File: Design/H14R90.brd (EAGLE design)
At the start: 34.6 x 30 mm, 39 parts, among them P2 HEXABIT_17.32_NO_P6, Q1 MMBT3904LT1, Q2 MMBT3904LT1, Q3 MMBT3904LT1, Q4 MMBT3904LT1, U1 STM32G0B1CEU6N, U2 LM2775-Q1, X1 XTALL_CSTCE8M00G52

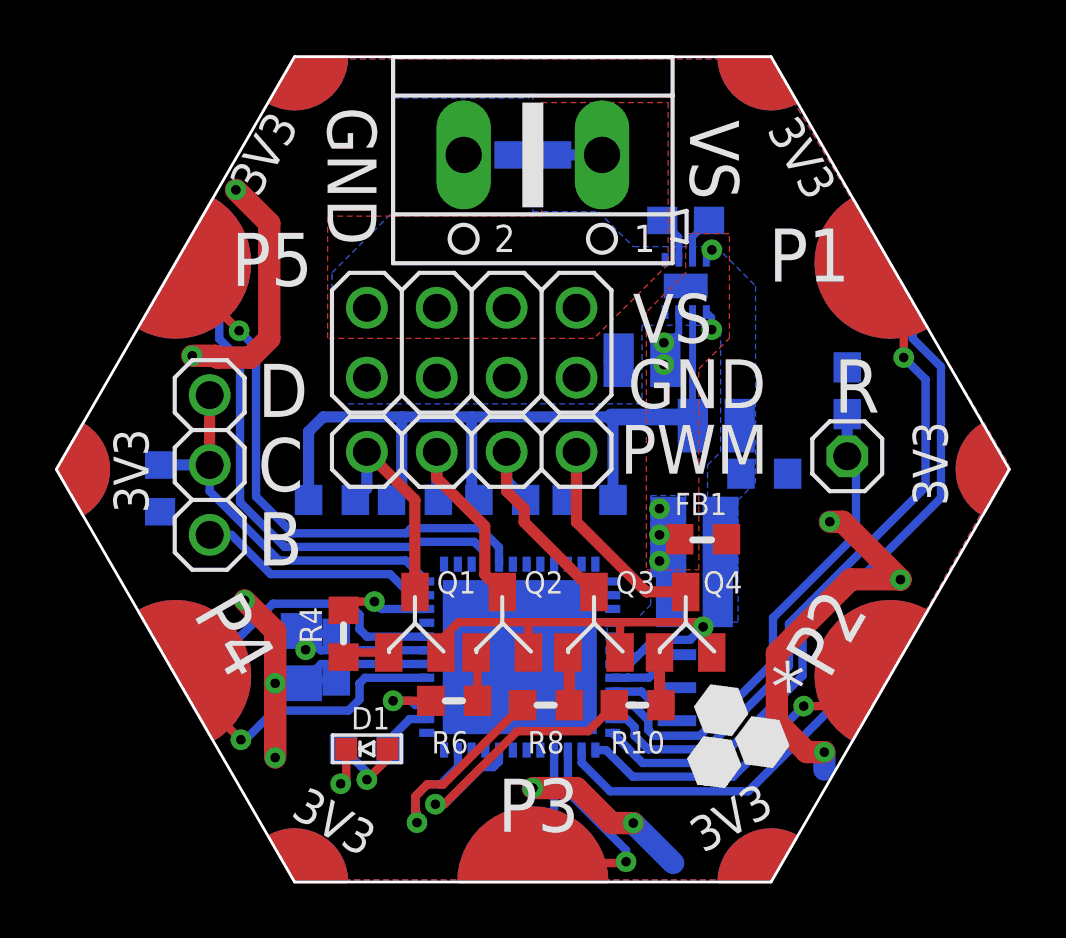
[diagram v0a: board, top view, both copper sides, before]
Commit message: -Fix the outputs pin headers spacing
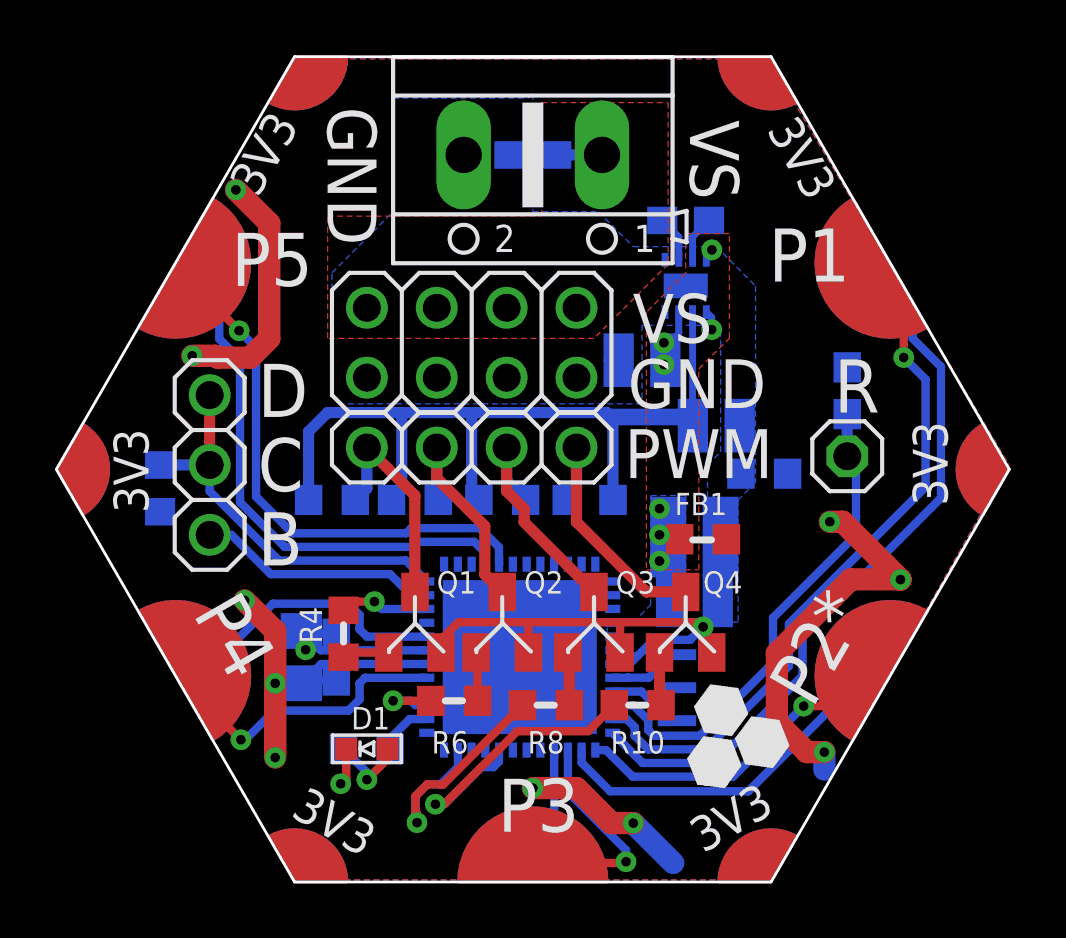
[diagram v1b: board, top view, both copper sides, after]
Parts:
- moved JP1 0.16 mm to (-2.22, 15.9)
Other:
- board text added: "7.2V Max"
- board text added: "P2*"
- board text removed: "*P2"
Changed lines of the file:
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@@
 <text x="8.5725" y="21.9075" size="1.9304" layer="21" rot="SR0">P1</text>
 <text x="11.1125" y="21.74875" size="1.9304" layer="26" rot="SMR0">P1</text>
-<text x="10.16" y="6.35" size="1.9304" layer="21" rot="R60">*P2</text>
-<text x="14.44625" y="9.36625" size="1.9304" layer="26" rot="MR0">*P2</text>
+<text x="10.16" y="6.35" size="1.9304" layer="21" rot="R60">P2*</text>
+<text x="14.12875" y="9.36625" size="1.9304" layer="26" rot="SMR0">P2*</text>
 <text x="-11.1125" y="23.65375" size="1.9304" layer="26" rot="MR180">P5</text>
 <text x="-10.95375" y="21.74875" size="1.9304" layer="21" rot="SR0">P5</text>
 <text x="-12.3825" y="9.8425" size="1.9304" layer="21" rot="SR300">P4</text>
-<text x="-13.6525" y="11.27125" size="1.9304" layer="26" rot="MR180">P4</text>
+<text x="-11.58875" y="9.2075" size="1.9304" layer="26" rot="MR0">P4</text>
 <text x="-1.5875" y="3.81" size="1.9304" layer="26" rot="MR180">P3</text>
 <text x="-1.27" y="1.905" size="1.9304" layer="21">P3</text>
-<text x="-2.2225" y="23.1775" size="1.9304" layer="22" font="vector" rot="MR180" align="center">H14R90</text>
+<text x="-9.8425" y="15.71625" size="1.9304" layer="22" font="vector" rot="MR90" align="center">H14R90</text>
 <text x="-10.00125" y="11.58875" size="1.9304" layer="25">B</text>
 <text x="10.95375" y="17.145" size="1.9304" layer="21">R</text>
@@
 <text x="3.6327875" y="19.685" size="1.778" layer="21">VS</text>
 <text x="3.451703125" y="17.30375" size="1.778" layer="21">GND</text>
-<text x="3.175" y="14.9225" size="1.778" layer="21">PWM</text>
+<text x="3.33375" y="14.76375" size="1.778" layer="21">PWM</text>
 <text x="-7.46125" y="28.2575" size="1.778" layer="21" rot="SR270">GND</text>
 <text x="5.715" y="27.78125" size="1.778" layer="21" rot="SR270">VS</text>
+<text x="-1.11125" y="23.33625" size="1.4224" layer="22" font="vector" rot="MR0" align="center">7.2V Max</text>
+<text x="3.4925" y="28.73375" size="1.27" layer="22" rot="SMR0">VS</text>
+<text x="-1.11125" y="28.73375" size="1.27" layer="22" rot="SMR0">GND</text>
 </plain>
 <attributes>
@@
 <attribute name="MFN" value="" x="-6.0325" y="4.92125" size="1.778" layer="28" rot="MR0" display="off"/>
 <attribute name="MPN" value="" x="-6.0325" y="4.92125" size="1.778" layer="28" rot="MR0" display="off"/>
-<attribute name="NAME" x="-5.3975" y="5.715" size="0.8128" layer="26" rot="MR0"/>
+<attribute name="NAME" x="-5.3975" y="5.55625" size="0.8128" layer="26" rot="MR0"/>
 <attribute name="OCTOPART_URL" value="" x="-6.0325" y="4.92125" size="1.778" layer="28" rot="MR0" display="off"/>
 <attribute name="RESISTANCE" value="" x="-6.0325" y="4.92125" size="1.778" layer="28" rot="MR0" display="off"/>
@@
 <attribute name="MFN" value="" x="-7.14375" y="8.255" size="1.778" layer="28" rot="MR270" display="off"/>
 <attribute name="MPN" value="" x="-7.14375" y="8.255" size="1.778" layer="28" rot="MR270" display="off"/>
-<attribute name="NAME" x="-6.429375" y="7.540625" size="0.8128" layer="26" rot="MR90"/>
+<attribute name="NAME" x="-6.270625" y="7.699375" size="0.8128" layer="26" rot="MR90"/>
 <attribute name="OCTOPART_URL" value="" x="-7.14375" y="8.255" size="1.778" layer="28" rot="MR270" display="off"/>
 <attribute name="TOLERANCE" value="" x="-7.14375" y="8.255" size="1.778" layer="28" rot="MR270" display="off"/>
@@
 <attribute name="MFN" value="" x="-8.41375" y="8.255" size="1.778" layer="28" rot="MR270" display="off"/>
 <attribute name="MPN" value="" x="-8.41375" y="8.255" size="1.778" layer="28" rot="MR270" display="off"/>
-<attribute name="NAME" x="-10.398125" y="7.77875" size="0.8128" layer="26" rot="MR90"/>
+<attribute name="NAME" x="-8.969375" y="5.23875" size="0.8128" layer="26" rot="MR90"/>
 <attribute name="OCTOPART_URL" value="" x="-8.41375" y="8.255" size="1.778" layer="28" rot="MR270" display="off"/>
 <attribute name="TOLERANCE" value="" x="-8.41375" y="8.255" size="1.778" layer="28" rot="MR270" display="off"/>
@@
 <attribute name="VOLTAGE_RATING" value="" x="11.43" y="17.93875" size="1.778" layer="28" rot="MR90" display="off"/>
 </element>
-<element name="JP1" library="pinhead" library_urn="urn:adsk.eagle:library:325" package="1X04" package3d_urn="urn:adsk.eagle:package:22407/2" value="" x="-2.2225" y="15.71625" smashed="yes">
-<attribute name="POPULARITY" value="91" x="-2.2225" y="15.71625" size="1.778" layer="27" display="off"/>
-<attribute name="VALUE" x="-7.3025" y="12.54125" size="1.27" layer="27"/>
+<element name="JP1" library="pinhead" library_urn="urn:adsk.eagle:library:325" package="1X04" package3d_urn="urn:adsk.eagle:package:22407/2" value="" x="-2.2225" y="15.875" smashed="yes">
+<attribute name="POPULARITY" value="91" x="-2.2225" y="15.875" size="1.778" layer="27" display="off"/>
+<attribute name="VALUE" x="-7.3025" y="12.7" size="1.27" layer="27"/>
 </element>
 <element name="JP2" library="pinhead" library_urn="urn:adsk.eagle:library:325" package="2X04" package3d_urn="urn:adsk.eagle:package:22461/2" value="" x="-2.2225" y="19.685" smashed="yes" rot="R180">
@@
 <contactref element="R7" pad="1"/>
 <wire x1="-8.1525" y1="13.97" x2="-8.1525" y2="16.45375" width="0.4064" layer="16"/>
-<wire x1="-8.1525" y1="16.45375" x2="-7.62" y2="16.98625" width="0.4064" layer="16"/>
-<wire x1="-7.62" y1="16.98625" x2="-4.7625" y2="16.98625" width="0.4064" layer="16"/>
-<wire x1="-4.7625" y1="16.98625" x2="-2.2225" y2="16.98625" width="0.4064" layer="16"/>
-<wire x1="-2.2225" y1="16.98625" x2="2.8575" y2="16.98625" width="0.4064" layer="16"/>
+<wire x1="-8.1525" y1="16.45375" x2="-7.46125" y2="17.145" width="0.4064" layer="16"/>
+<wire x1="-7.46125" y1="17.145" x2="-4.7625" y2="17.145" width="0.4064" layer="16"/>
+<wire x1="-4.7625" y1="17.145" x2="-2.2225" y2="17.145" width="0.4064" layer="16"/>
+<wire x1="-2.2225" y1="17.145" x2="2.69875" y2="17.145" width="0.4064" layer="16"/>
 <wire x1="2.91375" y1="13.97" x2="2.91375" y2="16.93" width="0.4064" layer="16"/>
 <wire x1="2.91375" y1="16.93" x2="2.8575" y2="16.98625" width="0.4064" layer="16"/>
+<wire x1="2.8575" y1="16.98625" x2="2.69875" y2="17.145" width="0.4064" layer="16"/>
 <wire x1="-1.96125" y1="13.97" x2="-2.2225" y2="14.23125" width="0.4064" layer="16"/>
-<wire x1="-2.2225" y1="14.23125" x2="-2.2225" y2="16.98625" width="0.4064" layer="16"/>
+<wire x1="-2.2225" y1="14.23125" x2="-2.2225" y2="17.145" width="0.4064" layer="16"/>
 <wire x1="-5.13625" y1="13.97" x2="-4.7625" y2="14.34375" width="0.4064" layer="16"/>
-<wire x1="-4.7625" y1="14.34375" x2="-4.7625" y2="16.98625" width="0.4064" layer="16"/>
+<wire x1="-4.7625" y1="14.34375" x2="-4.7625" y2="17.145" width="0.4064" layer="16"/>
 <wire x1="5.806253125" y1="20.79875" x2="5.806253125" y2="17.156246875" width="0.254" layer="16"/>
 <wire x1="5.806253125" y1="17.156246875" x2="5.8175" y2="17.145" width="0.254" layer="16"/>
@@
 <contactref element="R11" pad="2"/>
 <contactref element="Q4" pad="3"/>
-<wire x1="1.5875" y1="15.71625" x2="1.5875" y2="13.165" width="0.4064" layer="1"/>
+<wire x1="1.5875" y1="15.875" x2="1.5875" y2="13.165" width="0.4064" layer="1"/>
 <wire x1="4.1275" y1="10.625" x2="1.5875" y2="13.165" width="0.4064" layer="1"/>
 <wire x1="4.1275" y1="10.625" x2="5.55625" y2="10.625" width="0.4064" layer="1"/>
-<wire x1="1.5875" y1="15.71625" x2="1.5875" y2="14.34375" width="0.4064" layer="16"/>
+<wire x1="1.5875" y1="15.875" x2="1.5875" y2="14.34375" width="0.4064" layer="16"/>
 <wire x1="1.5875" y1="14.34375" x2="1.21375" y2="13.97" width="0.4064" layer="16"/>
 </signal>
@@
 <contactref element="R5" pad="2"/>
 <contactref element="Q1" pad="3"/>
-<wire x1="-6.0325" y1="15.71625" x2="-4.28625" y2="13.97" width="0.4064" layer="1"/>
-<wire x1="-4.28625" y1="13.97" x2="-4.28625" y2="10.625" width="0.4064" layer="1"/>
-<wire x1="-6.0325" y1="15.71625" x2="-6.0325" y2="14.39" width="0.4064" layer="16"/>
+<wire x1="-6.0325" y1="15.875" x2="-4.28625" y2="14.12875" width="0.4064" layer="1"/>
+<wire x1="-4.28625" y1="14.12875" x2="-4.28625" y2="10.625" width="0.4064" layer="1"/>
+<wire x1="-6.0325" y1="15.875" x2="-6.0325" y2="14.39" width="0.4064" layer="16"/>
 <wire x1="-6.0325" y1="14.39" x2="-6.4525" y2="13.97" width="0.4064" layer="16"/>
 </signal>
@@
 <contactref element="Q2" pad="3"/>
 <wire x1="-1.74625" y1="13.0175" x2="-3.4925" y2="14.76375" width="0.4064" layer="1"/>
-<wire x1="-3.4925" y1="15.71625" x2="-3.4925" y2="14.76375" width="0.4064" layer="1"/>
+<wire x1="-3.4925" y1="15.875" x2="-3.4925" y2="14.76375" width="0.4064" layer="1"/>
 <wire x1="-1.74625" y1="13.0175" x2="-1.74625" y2="11.26" width="0.4064" layer="1"/>
 <wire x1="-1.74625" y1="11.26" x2="-1.11125" y2="10.625" width="0.4064" layer="1"/>
-<wire x1="-3.4925" y1="15.71625" x2="-3.4925" y2="14.02625" width="0.4064" layer="16"/>
+<wire x1="-3.4925" y1="15.875" x2="-3.4925" y2="14.02625" width="0.4064" layer="16"/>
 <wire x1="-3.4925" y1="14.02625" x2="-3.43625" y2="13.97" width="0.4064" layer="16"/>
 </signal>
@@
 <contactref element="Q3" pad="3"/>
 <wire x1="-0.3175" y1="13.6525" x2="-0.9525" y2="14.2875" width="0.4064" layer="1"/>
-<wire x1="-0.9525" y1="15.71625" x2="-0.9525" y2="14.2875" width="0.4064" layer="1"/>
+<wire x1="-0.9525" y1="15.875" x2="-0.9525" y2="14.2875" width="0.4064" layer="1"/>
 <wire x1="-0.3175" y1="13.6525" x2="-0.3175" y2="13.165" width="0.4064" layer="1"/>
 <wire x1="-0.3175" y1="13.165" x2="2.2225" y2="10.625" width="0.4064" layer="1"/>
-<wire x1="-0.9525" y1="15.71625" x2="-0.9525" y2="14.66125" width="0.4064" layer="16"/>
+<wire x1="-0.9525" y1="15.875" x2="-0.9525" y2="14.66125" width="0.4064" layer="16"/>
 <wire x1="-0.9525" y1="14.66125" x2="-0.26125" y2="13.97" width="0.4064" layer="16"/>
 </signal>

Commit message: -Correcting some documentaion issues
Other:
- board text added: "P4*"
- board text removed: "P4"
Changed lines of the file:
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@@
 <rectangle x1="5.9683625" y1="3.629025" x2="7.08799375" y2="3.64375625" layer="21"/>
 <text x="8.5725" y="21.9075" size="1.9304" layer="21" rot="SR0">P1</text>
-<text x="11.1125" y="21.74875" size="1.9304" layer="26" rot="SMR0">P1</text>
+<text x="11.27125" y="23.1775" size="1.9304" layer="26" rot="SMR0">P1</text>
 <text x="10.16" y="6.35" size="1.9304" layer="21" rot="R60">P2*</text>
 <text x="14.12875" y="9.36625" size="1.9304" layer="26" rot="SMR0">P2*</text>
-<text x="-11.1125" y="23.65375" size="1.9304" layer="26" rot="MR180">P5</text>
+<text x="-11.27125" y="24.92375" size="1.9304" layer="26" rot="MR180">P5</text>
 <text x="-10.95375" y="21.74875" size="1.9304" layer="21" rot="SR0">P5</text>
-<text x="-12.3825" y="9.8425" size="1.9304" layer="21" rot="SR300">P4</text>
-<text x="-11.58875" y="9.2075" size="1.9304" layer="26" rot="MR0">P4</text>
+<text x="-12.3825" y="9.8425" size="1.9304" layer="21" rot="SR300">P4*</text>
+<text x="-9.8425" y="9.2075" size="1.9304" layer="26" rot="MR0">P4*</text>
 <text x="-1.5875" y="3.81" size="1.9304" layer="26" rot="MR180">P3</text>
 <text x="-1.27" y="1.905" size="1.9304" layer="21">P3</text>
-<text x="-9.8425" y="15.71625" size="1.9304" layer="22" font="vector" rot="MR90" align="center">H14R90</text>
+<text x="-10.00125" y="16.98625" size="1.9304" layer="22" font="vector" rot="MR90" align="center">H14R90</text>
 <text x="-10.00125" y="11.58875" size="1.9304" layer="25">B</text>
 <text x="10.95375" y="17.145" size="1.9304" layer="21">R</text>
